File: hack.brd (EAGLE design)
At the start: 44.5 x 26.9 mm, 40 parts, among them IC1 NUF2221W1T2G, IC3 LDO, IC4 ATSAMR21G, J1 USB-micro, SW1 SPST3.5X6MM, X1 TSX-3225 16 MHz, X2 MC-306 32.768 KHz

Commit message: Second commit
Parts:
- added B1: BALUN, hack:BALUN
- added C18, C19: 22pF, jack:C0402
- added JP4: (no value), pinhead:1X02
- moved C14 48.7 mm to (34.4, 16.8), turned to 90 degrees
- moved C15 40.4 mm to (19.6, 15.2), turned to 90 degrees
- moved X2 7.24 mm to (39.9, 8.64)
- moved C6 3.81 mm to (37.7, 17.1)
- moved L1 3.81 mm to (36.7, 18.9)
- moved C1 3.81 mm to (35.7, 14.9)
- moved C12 3.81 mm to (41.3, 14.9)
- moved C13 3.81 mm to (41.3, 12.1)
- moved X1 3.81 mm to (38.9, 13.6)
- moved R4 3.26 mm to (42.8, 13.7)
- moved C16 3.02 mm to (35.1, 7.11), turned to 90 degrees
- moved C17 3.02 mm to (35.1, 10.2), turned to 270 degrees
- moved C2 0.52 mm to (27.7, 19.6)
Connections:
- net N$4 renamed AVDD
- removed net 1: JP1.5
- removed net 14: JP2.15
- removed net 15: JP2.14
- removed net 16: JP2.13
- removed net 2: JP1.4
- removed net 3: JP1.3
- removed net 37: JP1.12
- removed net 38: JP1.11
- removed net 39: JP1.10
- removed net 41: JP1.8
- removed net 47: JP1.2
- removed net 48: JP1.1
- new net N$5: B1.3, C18.2
- new net N$6: B1.4, C19.2
- new net PA04: IC4.9, JP1.3
- new net PA05: IC4.10, JP1.2
- new net PA06: IC4.11, JP1.1
- new net PA07: IC4.12, JP2.15
- new net PA08: IC4.15, JP2.14
- new net PA09: IC4.16, JP2.13
- new net PA27: IC4.39, JP1.10
- new net PA28: IC4.41, JP1.8
- new net PB02: IC4.47, JP1.5
- new net PB03: IC4.48, JP1.4
- new net PB22: IC4.37, JP1.12
- new net PB23: IC4.38, JP1.11
- new net RFN: C18.1, IC4.19
- new net RFP: C19.1, IC4.18
- new net SMA: B1.1, JP4.1
- net !RESET: now also IC4.40
- net GND: now also B1.2, B1.5, B1.6, JP4.2
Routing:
- net VDD: track 12.6 -> 43.0 mm, vias 0 -> 2
- net !RESET: track 8.75 -> 34.0 mm, vias 0 -> 1
- net PA06: track 0.00 -> 24.9 mm, vias 0 -> 1
- net PA05: track 0.00 -> 22.6 mm, vias 0 -> 1
- net PA04: track 0.00 -> 20.3 mm, vias 0 -> 1
- net GND: track 21.9 -> 38.9 mm
- net PB02: track 0.00 -> 14.2 mm
- net PB22: track 0.00 -> 13.9 mm
- net VDDANA: track 6.07 -> 19.4 mm
- net PB03: track 0.00 -> 12.3 mm
- net PA07: track 0.00 -> 12.3 mm
- net PB23: track 0.00 -> 12.2 mm
- net PA09: track 0.00 -> 12.2 mm, vias 0 -> 1
- net 37: track 12.0 -> 0.00 mm
- net AGND: track 9.00 -> 20.7 mm
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
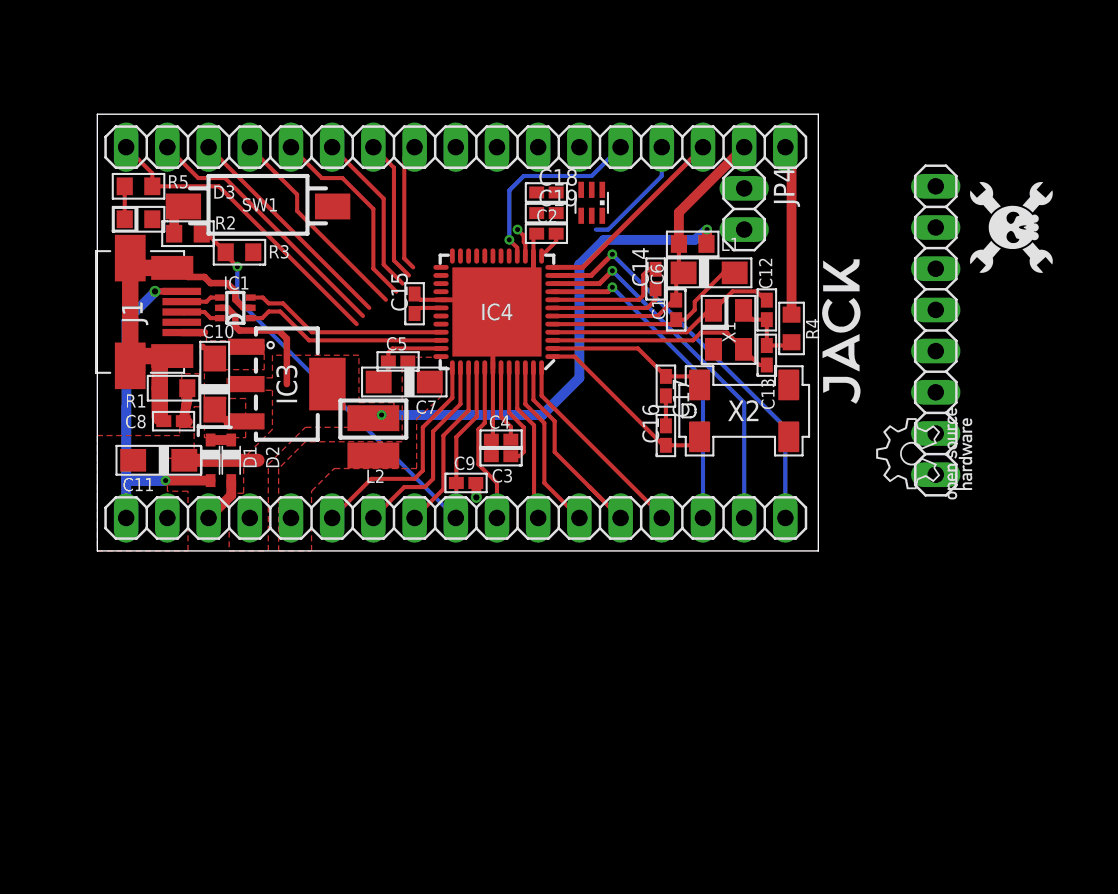
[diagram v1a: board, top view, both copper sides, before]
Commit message: Finishing layout, added PCB antenna
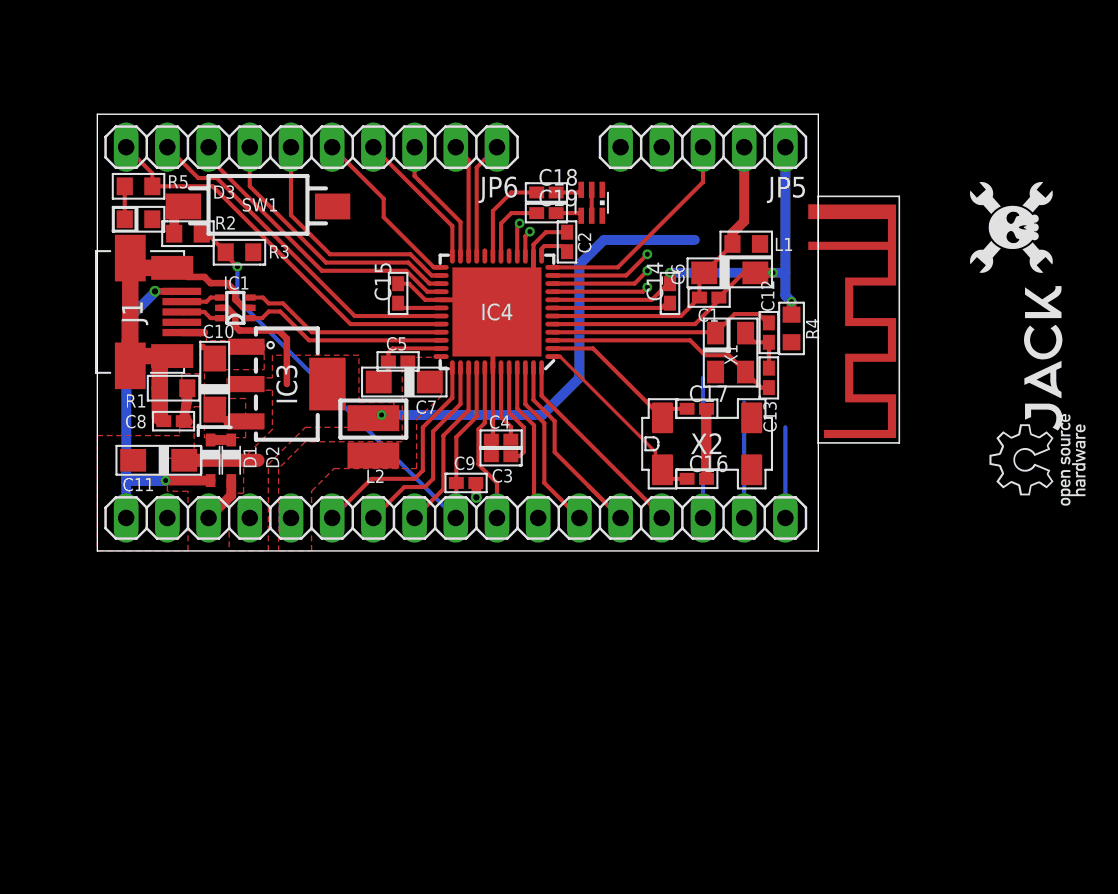
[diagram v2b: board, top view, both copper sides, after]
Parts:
- removed JP2: (no value), pinhead:1X17
- removed JP3: (no value), pinhead:1X08
- removed JP4: (no value), pinhead:1X02
- added ANT1: PCB-ANTENNA, hack:PCB-ANTENNA
- added JP5: (no value), pinhead:1X05
- added JP6: (no value), pinhead:1X10
- moved U$3 12.6 mm to (58.4, 11.6)
- moved U$6 7.00 mm to (57.8, 5.59)
- moved L1 3.30 mm to (40.0, 18.9)
- moved C16 3.28 mm to (37.0, 4.45), turned to 0 degrees
- moved X2 3.06 mm to (37.6, 6.60)
- moved C17 2.36 mm to (37.0, 8.76), turned to 0 degrees
- moved C1 2.17 mm to (37.7, 15.6), turned to 0 degrees
- moved C12 1.40 mm to (41.4, 13.5)
- moved C13 1.40 mm to (41.4, 10.7)
- moved X1 1.40 mm to (39.0, 12.2)
- moved C2 1.37 mm to (29.0, 19.1), turned to 90 degrees
- moved C6 1.27 mm to (39.0, 17.1)
- moved C14 1.26 mm to (35.3, 15.9)
- moved C15 1.20 mm to (18.5, 15.9)
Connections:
- removed net 10: JP3.5
- removed net 11: JP3.6
- removed net 12: JP3.7
- removed net 13: JP3.8
- removed net 19: JP2.12
- removed net 20: JP2.11
- removed net 21: JP2.10
- removed net 22: JP2.9
- removed net 25: JP2.8
- removed net 26: JP2.7
- removed net 27: JP2.6
- removed net 28: JP2.5
- removed net 29: JP2.4
- removed net 30: JP2.3
- removed net 31: JP2.2
- removed net 32: JP2.1, R5.2
- removed net 4: JP3.1
- removed net 7: JP3.3
- removed net 8: JP3.4
- removed net 9: JP3.2
- removed net GNDANA: JP2.17, R4.2
- removed net SMA: B1.1, JP4.1
- new net N$4: ANT1.ANT, B1.1
- new net PA12: IC4.21, JP6.1
- new net PA13: IC4.22, JP6.2
- new net PA14: IC4.23, JP6.3
- new net PA15: IC4.24, JP6.4
- new net PA16: IC4.25, JP6.5
- new net PA17: IC4.26, JP6.6
- new net PA18: IC4.27, JP6.7
- new net PA19: IC4.28, JP6.8
- new net PA22: IC4.31, JP6.9
- new net PA23: IC4.32, JP6.10, R5.2
- net AGND: now also JP5.1, R4.2
- net GND: now also ANT1.GND; no longer JP4.2
- net PA07: now also JP5.3; no longer JP2.15
- net PA08: now also JP5.4; no longer JP2.14
- net PA09: now also JP5.5; no longer JP2.13
- net VDDANA: now also JP5.2; no longer JP2.16
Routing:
- net PA23: track 0.00 -> 24.4 mm
- net PA22: track 0.00 -> 21.2 mm
- net AGND: track 20.7 -> 41.5 mm, vias 0 -> 3
- net 32: track 19.2 -> 0.00 mm
- net PA19: track 0.00 -> 18.4 mm
- net PA18: track 0.00 -> 16.7 mm
- net 31: track 16.4 -> 0.00 mm
- net PA17: track 0.00 -> 15.0 mm
- net 30: track 14.0 -> 0.00 mm
- net PA06: track 24.9 -> 11.9 mm
- net 29: track 12.9 -> 0.00 mm
- net 28: track 12.3 -> 0.00 mm
- net GNDANA: track 10.5 -> 0.00 mm
- net PA16: track 0.00 -> 10.4 mm
- net 27: track 10.2 -> 0.00 mm
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
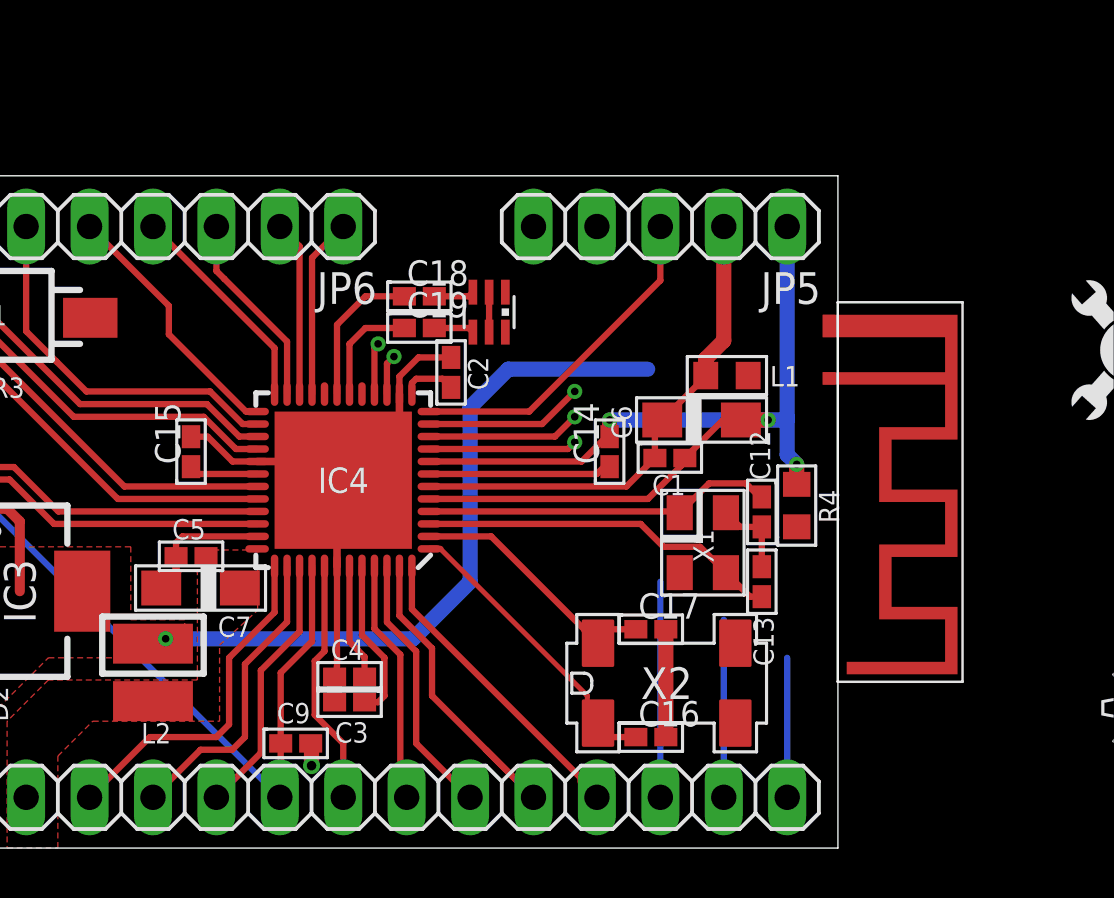
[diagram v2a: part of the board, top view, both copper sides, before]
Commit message: Third commit
Changed cutout of PCB so that one side hosts the antenna; moved part of
the header to the right side (use a female receptacle instead of a male
header to retain breadboard usability)
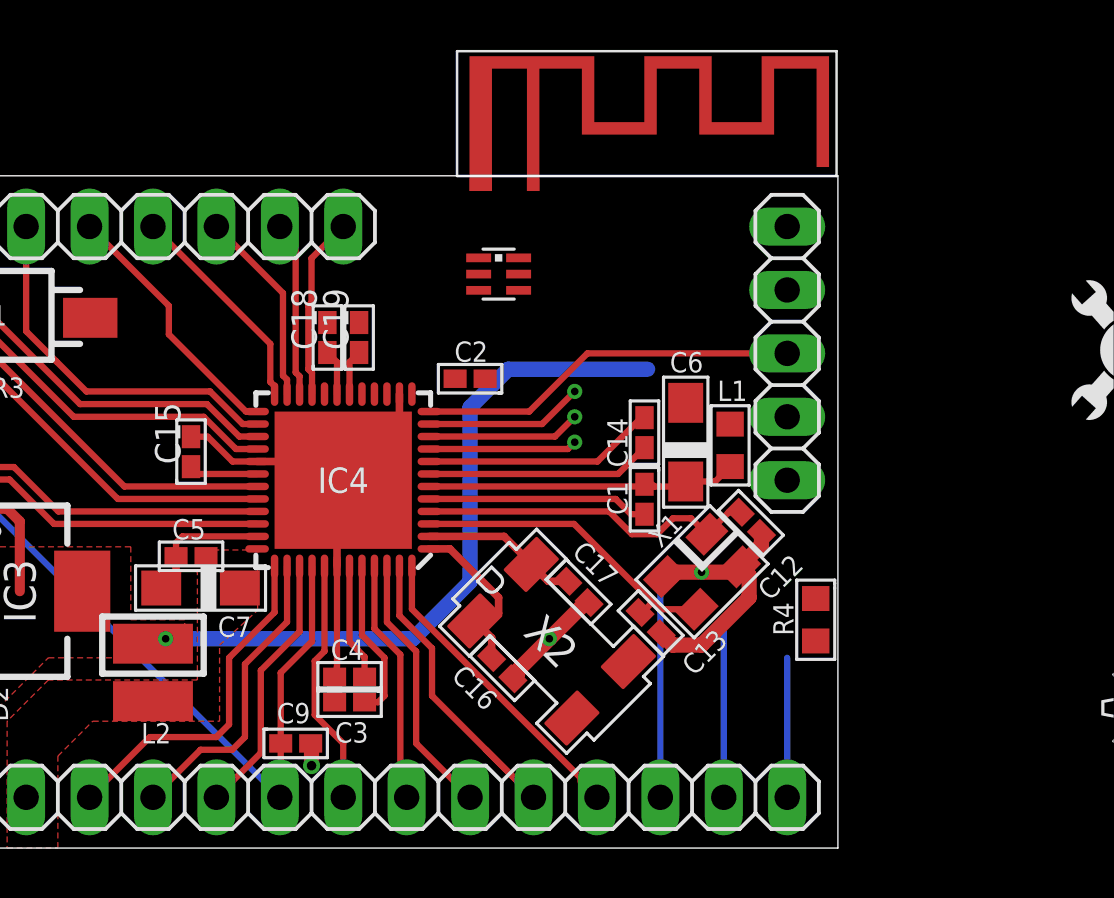
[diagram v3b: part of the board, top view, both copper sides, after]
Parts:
- moved ANT1 16.9 mm to (36.2, 28.6), turned to 0 degrees
- moved JP5 7.18 mm to (42.4, 19.8), turned to 90 degrees
- moved C16 6.56 mm to (31.0, 7.21), turned to 315 degrees
- moved X2 4.91 mm to (33.0, 8.28), turned to 315 degrees
- moved C13 4.75 mm to (36.9, 9.01), turned to 315 degrees
- moved R4 4.64 mm to (43.6, 9.14), turned to 270 degrees
- moved C18 4.04 mm to (24.0, 20.4), turned to 90 degrees
- moved C17 3.26 mm to (34.1, 10.3), turned to 315 degrees
- moved L1 2.80 mm to (40.1, 16.1), turned to 270 degrees
- moved C19 2.44 mm to (25.3, 20.4), turned to 90 degrees
- moved C1 1.94 mm to (36.7, 14.0), turned to 270 degrees
- moved C14 1.59 mm to (36.7, 16.6)
- moved B1 1.57 mm to (30.9, 23.0), turned to 90 degrees
- moved X1 1.16 mm to (39.0, 11.1), turned to 225 degrees
- moved C6 1.09 mm to (38.4, 16.3), turned to 90 degrees
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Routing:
- net AGND: track 41.5 -> 18.2 mm, vias 3 -> 0
- net VDDANA: track 19.9 -> 12.5 mm
- net XIN32: track 12.6 -> 7.04 mm
- net XOUT32: track 10.5 -> 6.31 mm
- net RFN: track 5.95 -> 1.82 mm
- net RFP: track 4.47 -> 1.82 mm
- net GND: track 44.5 -> 47.1 mm, vias 1 -> 3
- net VDDF: track 11.5 -> 9.23 mm
- net PA09: track 2.20 -> 0.00 mm, vias 1 -> 0
- net PA08: track 1.80 -> 0.00 mm, vias 1 -> 0
- net PA07: track 13.6 -> 15.3 mm
- net AVDD: track 7.43 -> 9.05 mm
- net N$5: track 1.61 -> 0.00 mm
- net N$6: track 1.61 -> 0.00 mm
- net XTAL2: track 14.5 -> 13.0 mm
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
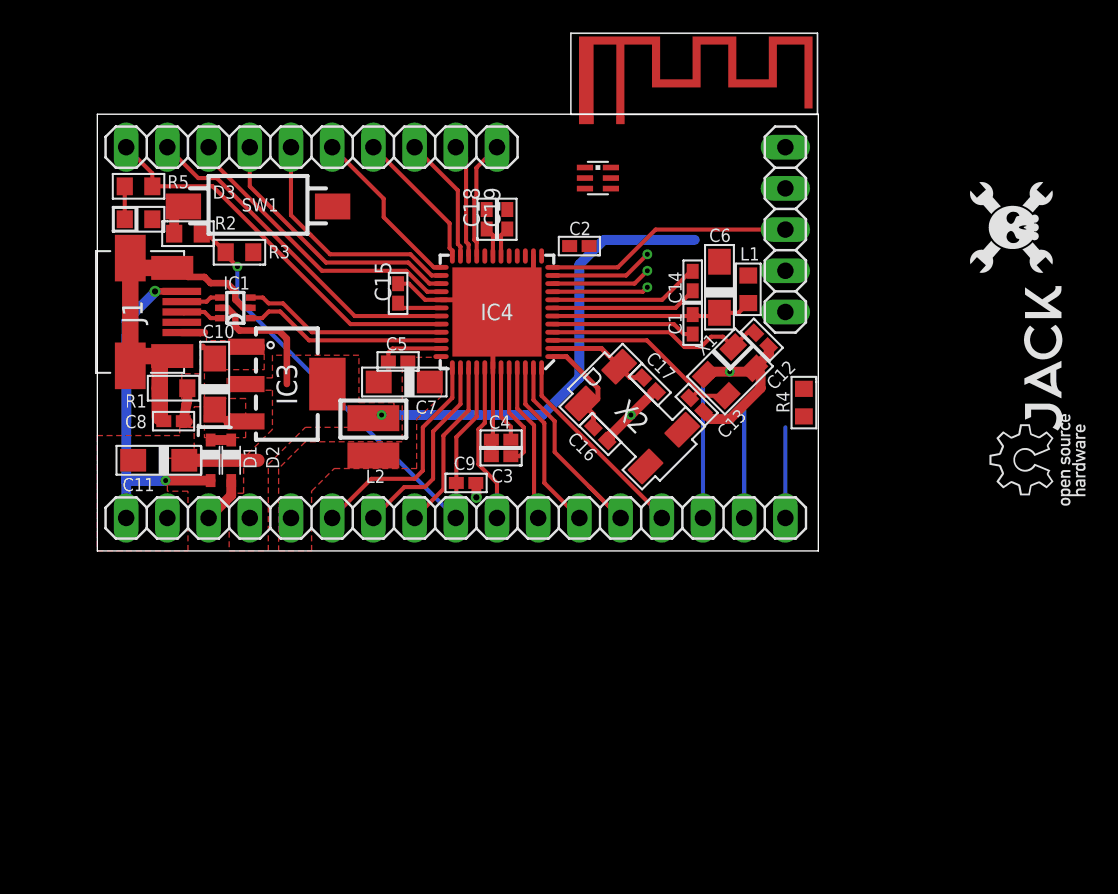
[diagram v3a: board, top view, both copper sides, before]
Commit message: Added impedance controlled microstrips
Added impedance controlled microstrips (diff. impedance of 100 Ohms from
chip to balun, single ended impedance of 50 Ohms from balun to antenna)
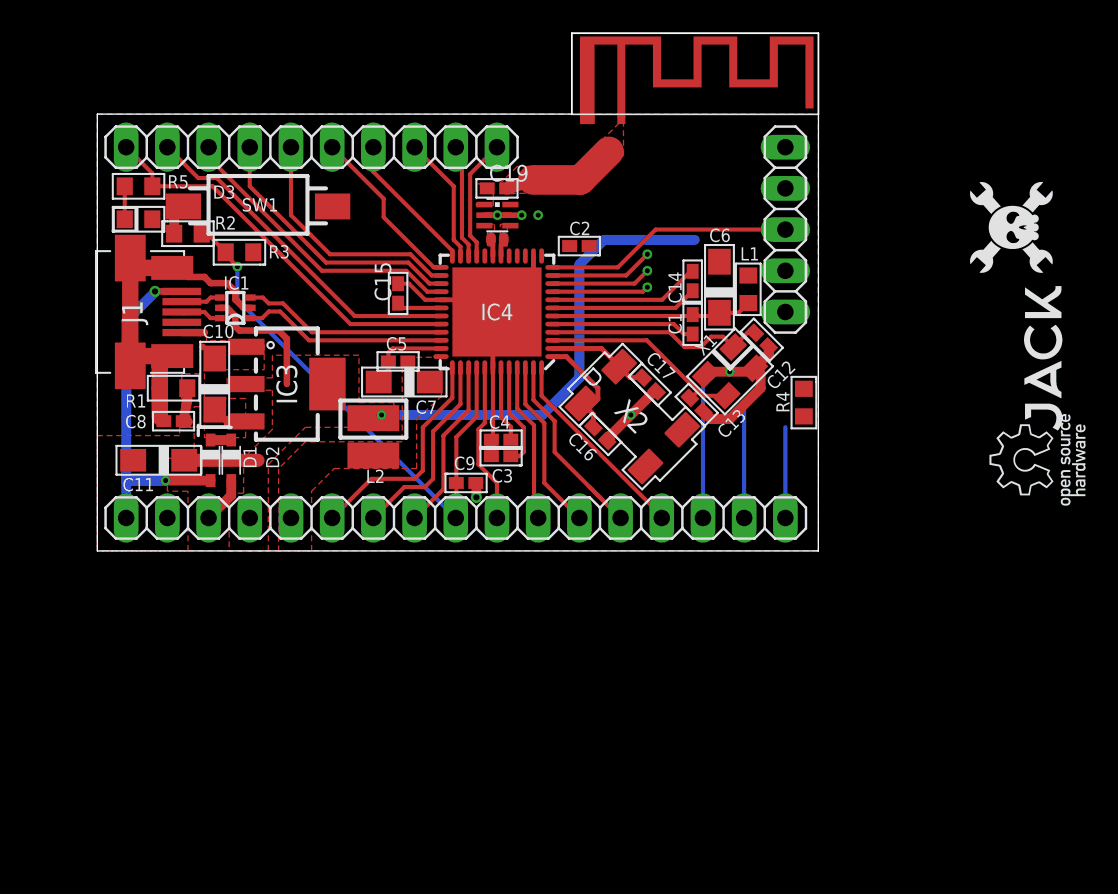
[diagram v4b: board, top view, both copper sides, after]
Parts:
- removed C18: 22pF, jack:C0402
- moved B1 6.61 mm to (24.7, 20.7)
- moved C19 2.01 mm to (24.6, 22.4), turned to 0 degrees
- moved ANT1 0.06 mm to (36.3, 28.6)
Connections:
- removed net N$4: ANT1.ANT, B1.1
- removed net N$6: B1.4, C19.2
- new net ANT: ANT1.ANT, C19.2
- net N$5: now also B1.1, C19.1; no longer B1.3, C18.2
- net RFN: now also B1.3; no longer C18.1
- net RFP: now also B1.4; no longer C19.1
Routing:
- net ANT: track 0.00 -> 7.12 mm
- net GND: track 47.1 -> 48.7 mm, vias 3 -> 6
- net RFN: track 1.82 -> 1.18 mm
- net RFP: track 1.82 -> 1.21 mm
- added copper zone on layer 1, net ANT
- added copper zone on layer 16, net GND
- added copper zone on layer 1, net N$5
- added copper zone on layer 1, net RFN
- added copper zone on layer 1, net RFP
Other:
- board size 44.5 x 26.9 mm -> 44.5 x 31.9 mm

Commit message: 1st revision board is done
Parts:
- removed R4: 0, jack:R0603
- removed U$3: JACK-LOGO, jack:JACK-LOGO
- added LOGO1: HACK-LOGO, hack:HACK-LOGO
- moved U$6 27.3 mm to (32.9, 16.8), turned to 0 degrees
- moved U$5 23.9 mm to (32.9, 21.2), turned to 0 degrees
- moved C2 0.95 mm to (28.8, 18.9)
- moved C19 0.26 mm to (24.6, 22.6)
- moved B1 0.26 mm to (24.6, 21.0)
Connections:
- removed net AGND: C1.2, C14.2, C6.-, IC4.17, IC4.20, IC4.5, IC4.8, JP5.1, R4.2
- net GND: now also C1.2, C14.2, C6.-, IC4.17, IC4.20, IC4.5, IC4.8, JP5.1; no longer R4.1
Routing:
- net VDDF: track 9.23 -> 57.5 mm, vias 0 -> 6
- net GND: track 48.7 -> 69.3 mm, vias 6 -> 93
- net PA09: track 0.00 -> 19.8 mm
- net AGND: track 18.2 -> 0.00 mm
- net PA08: track 0.00 -> 18.1 mm
- net PA06: track 11.9 -> 26.8 mm, vias 1 -> 2
- net PA05: track 13.3 -> 24.7 mm, vias 1 -> 2
- net VDD: track 41.1 -> 52.2 mm, vias 1 -> 2
- net PA04: track 14.6 -> 22.7 mm, vias 1 -> 2
- net VDDANA: track 12.5 -> 15.8 mm
- net RFN: track 1.18 -> 2.04 mm
